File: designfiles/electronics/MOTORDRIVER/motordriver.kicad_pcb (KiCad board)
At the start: 4 copper layers, 416 parts, among them IC1 LM5109BSDX_NOPB, IC10 LM5109BSDX_NOPB, IC11 LM5109BSDX_NOPB, IC12 LM5109BSDX_NOPB, IC13 INA2181A2IDGSR, IC14 LM5109BSDX_NOPB, IC15 LM5109BSDX_NOPB, IC16 LM5109BSDX_NOPB, IC17 LM5109BSDX_NOPB, IC18 INA2181A2IDGSR, IC2 LM5109BSDX_NOPB, IC3 LM5109BSDX_NOPB, IC4 LM5109BSDX_NOPB, IC5 INA2181A2IDGSR, IC6 BQ24133RGYR, IC7 LM5176PWPR, IC8 ATSAME53J18A-MF, IC9 LM5109BSDX_NOPB, J1 IMU1, J2 IMU2, J3 Conn_01x04_Socket, J4 Screw_Terminal_01x02, J5 1-84952-1, J6 1-84952-1, J7 1-84952-1, P1 USB_C_Plug_USB2.0, Q1 30V 71A, Q10 40V 70A, Q11 30V 71A, Q12 30V 71A, Q13 30V 71A, Q14 30V 71A, Q15 30V 71A, Q16 30V 71A, Q17 30V 71A, Q18 30V 71A, Q19 30V 71A, Q2 30V 71A, Q20 30V 71A, Q21 30V 71A, Q22 30V 71A, Q23 30V 71A, Q24 30V 71A, Q25 30V 71A, Q26 30V 71A, Q27 30V 71A, Q28 30V 71A, Q3 30V 71A, Q4 30V 71A, Q5 30V 71A, Q6 30V 71A, Q7 30V 71A, Q8 30V 71A, Q9 30V 71A, SW1 SW_DPST_x2, U1 LD1117S25TR_SOT223, U2 LD1117S33TR_SOT223, U3 LD1117S50TR_SOT223, U4 TMC4671-LA, U5 ATSAMD11D14A-M, U6 TMC4671-LA, U7 TMC4671-LA

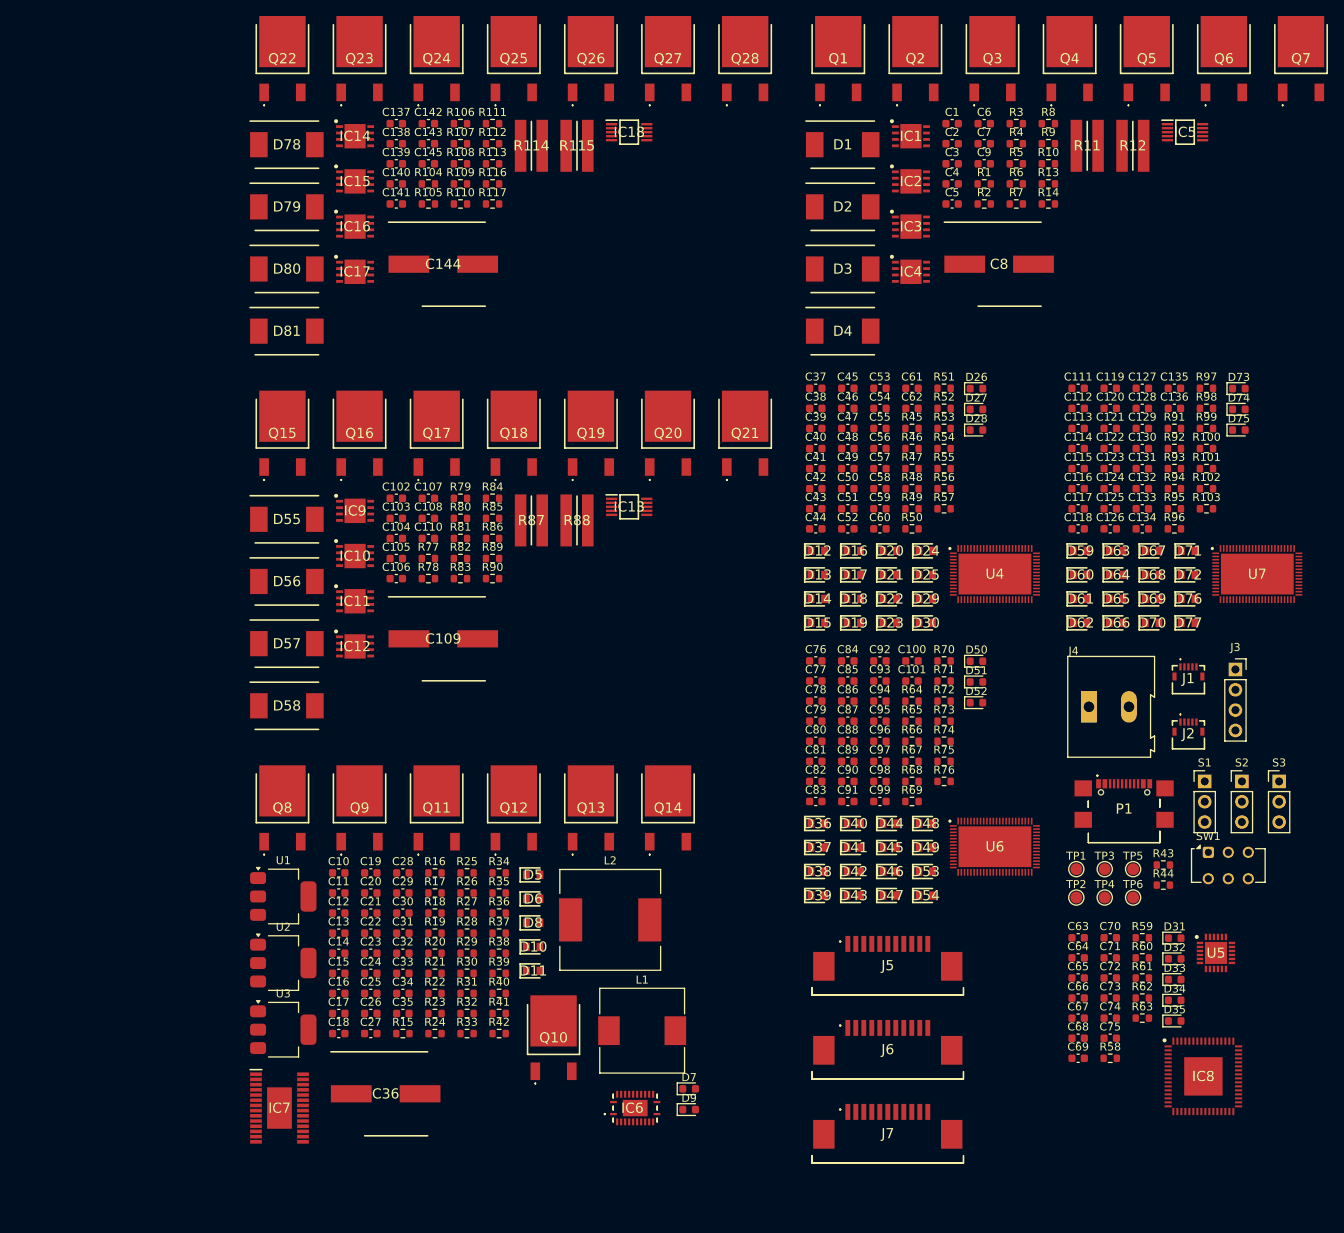
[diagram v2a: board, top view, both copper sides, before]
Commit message: added inductors
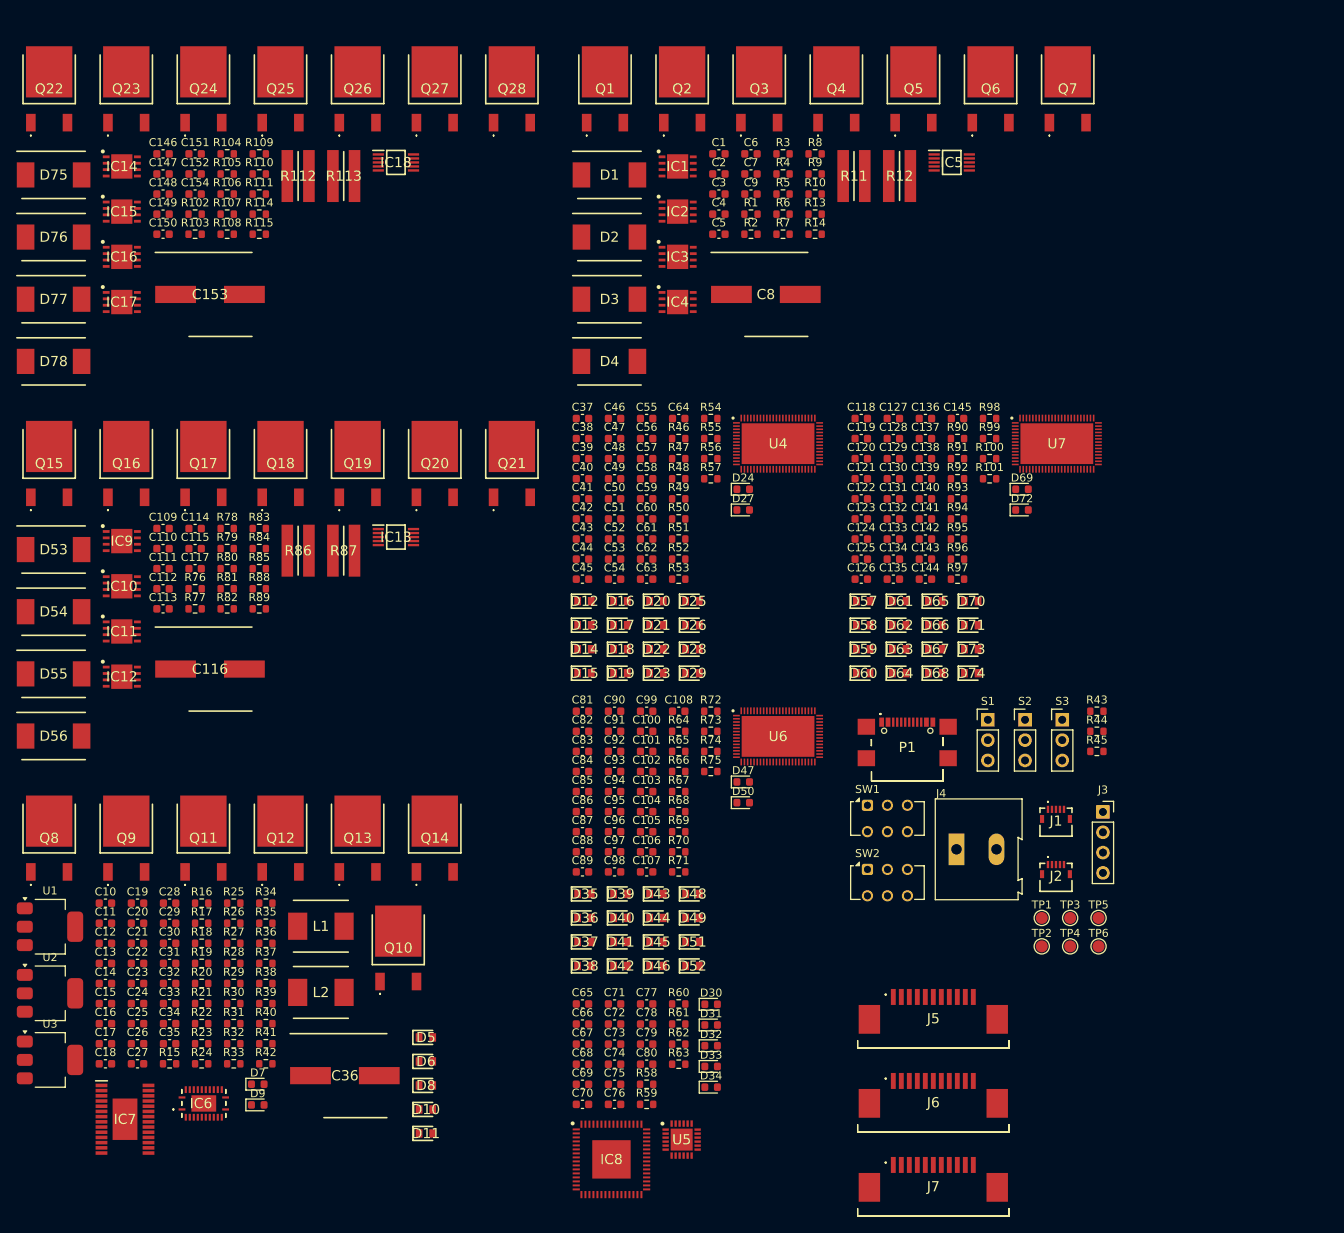
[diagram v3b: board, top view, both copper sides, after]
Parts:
- removed D79, D80, D81: 4A 40V, kuben-footprints:DIOM7959X262N
- removed R116, R117: 0.01Ω, Resistor_SMD:R_0603_1608Metric
- added C146: 0.1µF, Capacitor_SMD:C_0603_1608Metric, F.Cu at (58.1, 37.4)
- added C147: 1µF, Capacitor_SMD:C_0603_1608Metric, F.Cu at (58.1, 40.0)
- added C148: 1µF, Capacitor_SMD:C_0603_1608Metric, F.Cu at (58.1, 42.5)
- added C149: 0.1µF, Capacitor_SMD:C_0603_1608Metric, F.Cu at (58.1, 45.0)
- added C150: 1µF, Capacitor_SMD:C_0603_1608Metric, F.Cu at (58.1, 47.5)
- added C151: 0.1µF, Capacitor_SMD:C_0603_1608Metric, F.Cu at (62.1, 37.4)
- added C152: 1µF, Capacitor_SMD:C_0603_1608Metric, F.Cu at (62.1, 40.0)
- added C153: 220µF 35V, kuben-footprints:CAPAE1050X1050N, F.Cu at (64.0, 55.0)
- added C154: 0.1µF, Capacitor_SMD:C_0603_1608Metric, F.Cu at (62.1, 42.5)
- added SW2: SW_DPST_x2, Button_Switch_THT:SW_CK_JS202011AQN_DPDT_Angled, F.Cu at (146.1, 126.9)
- C100, C123, C127, C131, C59, C75, C90, C94: value 4.7µF -> 100nF
- C101, C62: value 10nF -> 4.7µF
- C102, C105, C142: value 0.1µF -> 470nF
- C103, C108: value 1µF -> 100nF
- C104, C106, C138, C141, C143: value 1µF -> 4.7µF
- C107: value 0.1µF -> 10nF
- C109: value 220µF 35V -> 0.1µF; footprint kuben-footprints:CAPAE1050X1050N -> Capacitor_SMD:C_0603_1608Metric
- C110: value 0.1µF -> 1µF
- C111, C113, C115: value 100nF -> 1µF
- C112, C114, C117: value 100nF -> 0.1µF
- C116: value 100nF -> 220µF 35V; footprint Capacitor_SMD:C_0603_1608Metric -> kuben-footprints:CAPAE1050X1050N
- C118, C120, C121, C46, C83, C86: value 100pF -> 100nF
- C122, C41, C45: value 100nF -> 100pF
- C124, C50, C56: value 470nF -> 100nF
- C125, C88: value 4.7µF -> 100pF
- C126, C89: value 470nF -> 100pF
- C128, C130, C52, C54, C60, C91, C93: value 470nF -> 4.7µF
- C129, C51, C53, C55, C61, C92: value 4.7µF -> 470nF
- C136: value 10nF -> 470nF
- C137, C140, C145: value 0.1µF -> 100nF
- C139: value 1µF -> 470nF
- C144: value 220µF 35V -> 10nF; footprint kuben-footprints:CAPAE1050X1050N -> Capacitor_SMD:C_0603_1608Metric
- C47: value 100pF -> 4.7µF
- C48: value 100nF -> 470nF
- C63: value 100nF -> 10nF
- C64, C68, C70, C72: value 10µF -> 100nF
- C67, C69, C71, C73, C76: value 100nF -> 10µF
- C78: value 100nF -> 4.7µF
- D24, D30, D47, D69, D72: value 4.7Vf 0.5A -> LED; footprint kuben-footprints:DIOC1709X85N -> Diode_SMD:D_0603_1608Metric
- D26, D28, D35, D51, D52, D73, D74: value LED -> 4.7Vf 0.5A; footprint Diode_SMD:D_0603_1608Metric -> kuben-footprints:DIOC1709X85N
- D53, D54, D76, D77: value 4.7Vf 0.5A -> 4A 40V; footprint kuben-footprints:DIOC1709X85N -> kuben-footprints:DIOM7959X262N
- D57, D58: value 4A 40V -> 4.7Vf 0.5A; footprint kuben-footprints:DIOM7959X262N -> kuben-footprints:DIOC1709X85N
- D75: value LED -> 4A 40V; footprint Diode_SMD:D_0603_1608Metric -> kuben-footprints:DIOM7959X262N
- L1: footprint Inductor_SMD:L_10.4x10.4_H4.8 -> kuben-footprints:INDPM6965X300N
- L2: value 1µH 420µΩ -> 1µH 22A; footprint Inductor_SMD:L_12x12mm_H8mm -> kuben-footprints:INDPM6965X300N
- R100: value 10kΩ -> 100kΩ
- R101: value 1kΩ -> 20kΩ
- R102: value 100kΩ -> 5Ω
- R103: value 20kΩ -> 4.7Ω
- R104, R107, R110, R77, R80, R83: value 5Ω -> 4.7Ω
- R105, R108, R79, R82: value 4.7Ω -> 5Ω
- R112, R113, R86: value 4.7Ω -> 10Ω 2W; footprint Resistor_SMD:R_0603_1608Metric -> kuben-footprints:RESC3263X80N
- R114, R115, R88: value 10Ω 2W -> 0.01Ω; footprint kuben-footprints:RESC3263X80N -> Resistor_SMD:R_0603_1608Metric
- R45: value 4.7kΩ -> 10K
- R48: value 1kΩ -> 4.7kΩ
- R51, R73, R97: value 10kΩ -> 1kΩ
- R52, R72, R96, R98: value 1kΩ -> 10kΩ
- R74: value 1kΩ -> 100kΩ
- R75: value 100kΩ -> 20kΩ
- R76: value 20kΩ -> 5Ω
- R90: value 0.01Ω -> 4.7kΩ
- R93: value 4.7kΩ -> 1kΩ
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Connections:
- net /driverIC/ADC_I0_POS renamed /servo1/ADC_I0_POS
- net /driverIC/ADC_I1_POS renamed /servo1/ADC_I1_POS
- net /driverIC/BRAKE renamed /drivergates1/BRAKE
- net /driverIC1/BRAKE renamed /drivergates2/BRAKE
- net /driverIC2/BRAKE renamed /drivergates3/BRAKE
- C100 pad 2: +3.3V -> Net-(U6-VCCCORE2)
- C101 pad 2: Net-(D53-A) -> +3.3V
- C102 pad 1: Net-(IC9-HS) -> GND
- C102 pad 2: Net-(D55-K) -> +3.3V
- C103 pad 1: +12V -> GND
- C103 pad 2: GND -> Net-(U6-VCCCORE1)
- C104 pad 1: +12V -> GND
- C104 pad 2: GND -> +3.3V
- C105 pad 1: Net-(IC10-HS) -> GND
- C105 pad 2: Net-(D56-K) -> +3.3V
- C106 pad 1: +12V -> GND
- C106 pad 2: GND -> +5V
- C107 pad 1: Net-(IC12-HS) -> GND
- C107 pad 2: Net-(D57-K) -> Net-(D51-A)
- C108 pad 1: +12V -> GND
- C108 pad 2: GND -> +5V
- C109 pad 1: +12V -> Net-(IC9-HS)
- C109 pad 2: GND -> Net-(D53-K)
- C110 pad 1: GND -> +12V
- C110 pad 2: +5V -> GND
- C111 pad 1: GND -> +12V
- C111 pad 2: +3.3V -> GND
- C112 pad 1: GND -> Net-(IC10-HS)
- C112 pad 2: +3.3V -> Net-(D54-K)
- C113 pad 1: GND -> +12V
- C113 pad 2: +3.3V -> GND
- C114 pad 1: GND -> Net-(IC12-HS)
- C114 pad 2: +3.3V -> Net-(D55-K)
- C115 pad 1: GND -> +12V
- C115 pad 2: +3.3V -> GND
- C116 pad 1: GND -> +12V
- C116 pad 2: +3.3V -> GND
- C117 pad 2: +3.3V -> +5V
- C118 pad 2: /driverIC2/HALL_U -> +3.3V
- C120 pad 2: /driverIC2/HALL_V -> +3.3V
- C121 pad 2: /driverIC2/HALL_W -> +3.3V
- C122 pad 2: +3.3V -> /servo3/HALL_U
- C124 pad 2: +3.3V -> Net-(U7-VCCCORE3)
- C125 pad 2: +3.3V -> /servo3/HALL_V
- C126 pad 2: +3.3V -> /servo3/HALL_W
- C131 pad 1: GND -> Net-(U7-NRST)
- C131 pad 2: +3.3V -> GND
- C136 pad 2: Net-(D76-A) -> +3.3V
- C137 pad 1: Net-(IC14-HS) -> GND
- C137 pad 2: Net-(D78-K) -> Net-(U7-VCCCORE2)
- C138 pad 1: +12V -> GND
- C138 pad 2: GND -> +3.3V
- C139 pad 1: +12V -> GND
- C139 pad 2: GND -> +3.3V
- C140 pad 1: Net-(IC15-HS) -> GND
- C140 pad 2: Net-(D79-K) -> Net-(U7-VCCCORE1)
- C141 pad 1: +12V -> GND
- C141 pad 2: GND -> +3.3V
- C142 pad 1: Net-(IC17-HS) -> GND
- C142 pad 2: Net-(D80-K) -> +3.3V
- C143 pad 1: +12V -> GND
- C143 pad 2: GND -> +5V
- C144 pad 1: +12V -> GND
- C144 pad 2: GND -> Net-(D73-A)
- C41 pad 2: +3.3V -> /servo1/HALL_U
- C43 pad 2: +3.3V -> Net-(U4-VCCCORE3)
- C44 pad 2: /driverIC/HALL_U -> /servo1/HALL_V
- C45 pad 2: +3.3V -> /servo1/HALL_W
- C46 pad 2: /driverIC/HALL_V -> +3.3V
- C47 pad 2: /driverIC/HALL_W -> +3.3V
- C50 pad 1: GND -> Net-(U4-NRST)
- C50 pad 2: +3.3V -> GND
- C56 pad 2: +3.3V -> Net-(U4-VCCCORE2)
- C59 pad 2: +3.3V -> Net-(U4-VCCCORE1)
- C62 pad 2: Net-(D29-A) -> +5V
- C63 pad 1: +3.3V -> GND
- C63 pad 2: GND -> Net-(D28-A)
- C64 pad 1: +3.3V -> GND
- C64 pad 2: GND -> +5V
- C74 pad 1: Net-(IC8-VDDCORE) -> +3.3V
- C75 pad 1: Net-(IC8-VDDCORE) -> +3.3V
- C76 pad 1: GND -> +3.3V
- C76 pad 2: +3.3V -> GND
- C77 pad 2: +3.3V -> Net-(IC8-VDDCORE)
- C78 pad 2: +3.3V -> Net-(IC8-VDDCORE)
- C79 pad 1: GND -> /IO/RESETN
- C79 pad 2: +3.3V -> GND
- C80 pad 1: GND -> +3.3V
- C80 pad 2: +3.3V -> GND
- C83 pad 2: /driverIC1/HALL_U -> +3.3V
- C85 pad 2: /driverIC1/HALL_V -> /servo2/HALL_U
- C86 pad 2: /driverIC1/HALL_W -> +3.3V
- C87 pad 2: +3.3V -> Net-(U6-VCCCORE3)
- C88 pad 2: +3.3V -> /servo2/HALL_V
- C89 pad 2: +3.3V -> /servo2/HALL_W
- C94 pad 1: GND -> Net-(U6-NRST)
- C94 pad 2: +3.3V -> GND
- D20 pad 2: /driverIC/HALL_W -> /servo1/HALL_W
- D21 pad 1: /driverIC/HALL_W -> /servo1/HALL_W
- D22 pad 2: /driverIC/HALL_V -> /servo1/HALL_V
- D23 pad 1: /driverIC/HALL_V -> /servo1/HALL_V
- D24 pad 1: +5V -> GND
- D24 pad 2: /driverIC/HALL_U -> Net-(D24-A)
- D25 pad 1: /driverIC/HALL_U -> +5V
- D25 pad 2: GND -> /servo1/HALL_U
- D26 pad 1: GND -> /servo1/HALL_U
- D26 pad 2: Net-(D26-A) -> GND
- D28 pad 1: GND -> +5V
- D29 pad 1: +5V -> Net-(D28-A)
- D29 pad 2: Net-(D29-A) -> GND
- D30 pad 1: Net-(D29-A) -> GND
- D30 pad 2: GND -> Net-(D30-A)
- D35 pad 1: GND -> +5V
- D35 pad 2: Net-(D35-A) -> /servo2/ADC_I0_POS
- D36 pad 1: +5V -> /servo2/ADC_I0_POS
- D36 pad 2: /driverIC1/ADC_I0_POS -> GND
- D37 pad 1: /driverIC1/ADC_I0_POS -> +5V
- D37 pad 2: GND -> /servo2/ADC_I1_POS
- D38 pad 1: +5V -> /servo2/ADC_I1_POS
- D38 pad 2: /driverIC1/ADC_I1_POS -> GND
- D39 pad 1: /driverIC1/ADC_I1_POS -> +5V
- D39 pad 2: GND -> +2.5V
- D40 pad 1: +5V -> +2.5V
- D40 pad 2: +2.5V -> GND
- D41 pad 1: +2.5V -> +5V
- D41 pad 2: GND -> +2.5V
- D42 pad 1: +5V -> +2.5V
- D42 pad 2: +2.5V -> GND
- D43 pad 1: +2.5V -> +5V
- D43 pad 2: GND -> /servo2/HALL_W
- D44 pad 1: +5V -> /servo2/HALL_W
- D44 pad 2: /driverIC1/HALL_W -> GND
- D45 pad 1: /driverIC1/HALL_W -> +5V
- D45 pad 2: GND -> /servo2/HALL_V
- D46 pad 1: +5V -> /servo2/HALL_V
- D46 pad 2: /driverIC1/HALL_V -> GND
- D47 pad 1: /driverIC1/HALL_V -> GND
- D47 pad 2: GND -> Net-(D47-A)
- D48 pad 2: /driverIC1/HALL_U -> /servo2/HALL_U
- D49 pad 1: /driverIC1/HALL_U -> /servo2/HALL_U
- D51 pad 1: GND -> +5V
- D52 pad 1: GND -> Net-(D51-A)
- D52 pad 2: Net-(D52-A) -> GND
- D53 pad 1: +5V -> Net-(D53-K)
- D54 pad 1: Net-(D53-A) -> Net-(D54-K)
- D54 pad 2: GND -> Net-(D54-A)
- D56 pad 1: Net-(D56-K) -> +12V
- D57 pad 1: Net-(D57-K) -> +5V
- D57 pad 2: Net-(D57-A) -> /servo3/ADC_I0_POS
- D58 pad 1: +12V -> /servo3/ADC_I0_POS
- D58 pad 2: Net-(D58-A) -> GND
- D59 pad 2: /driverIC2/ADC_I0_POS -> /servo3/ADC_I1_POS
- D60 pad 1: /driverIC2/ADC_I0_POS -> /servo3/ADC_I1_POS
- D61 pad 2: /driverIC2/ADC_I1_POS -> +2.5V
- D62 pad 1: /driverIC2/ADC_I1_POS -> +2.5V
- D65 pad 2: +2.5V -> /servo3/HALL_W
- D66 pad 1: +2.5V -> /servo3/HALL_W
- D67 pad 2: /driverIC2/HALL_W -> /servo3/HALL_V
- D68 pad 1: /driverIC2/HALL_W -> /servo3/HALL_V
- D69 pad 1: +5V -> GND
- D69 pad 2: /driverIC2/HALL_V -> Net-(D69-A)
- D70 pad 1: /driverIC2/HALL_V -> +5V
- D70 pad 2: GND -> /servo3/HALL_U
- D71 pad 1: +5V -> /servo3/HALL_U
- D71 pad 2: /driverIC2/HALL_U -> GND
- D72 pad 1: /driverIC2/HALL_U -> GND
- D72 pad 2: GND -> Net-(D72-A)
- D73 pad 1: GND -> +5V
- D74 pad 1: GND -> Net-(D73-A)
- D74 pad 2: Net-(D74-A) -> GND
- D75 pad 1: GND -> Net-(D75-K)
- D76 pad 1: +5V -> Net-(D76-K)
- D77 pad 1: Net-(D76-A) -> Net-(D77-K)
- D77 pad 2: GND -> Net-(D77-A)
- D78 pad 1: Net-(D78-K) -> +12V
- IC1 pad 2: /drivergates/PWM_W_H -> /drivergates1/PWM_W_H
- IC1 pad 3: /drivergates/PWM_W_L -> /drivergates1/PWM_W_L
- IC10 pad 2: /drivergates1/PWM_V_H -> /drivergates2/PWM_V_H
- IC10 pad 3: /drivergates1/PWM_V_L -> /drivergates2/PWM_V_L
- IC10 pad 8: Net-(D56-K) -> Net-(D54-K)
- IC12 pad 2: /drivergates1/PWM_U_H -> /drivergates2/PWM_U_H
- IC12 pad 3: /drivergates1/PWM_U_L -> /drivergates2/PWM_U_L
- IC12 pad 8: Net-(D57-K) -> Net-(D55-K)
- IC13 pad 1: /driverIC1/ADC_I0_POS -> /servo2/ADC_I0_POS
- IC13 pad 9: /driverIC1/ADC_I1_POS -> /servo2/ADC_I1_POS
- IC14 pad 2: /drivergates2/PWM_W_H -> /drivergates3/PWM_W_H
- IC14 pad 3: /drivergates2/PWM_W_L -> /drivergates3/PWM_W_L
- IC14 pad 8: Net-(D78-K) -> Net-(D75-K)
- IC15 pad 2: /drivergates2/PWM_V_H -> /drivergates3/PWM_V_H
- IC15 pad 3: /drivergates2/PWM_V_L -> /drivergates3/PWM_V_L
- IC15 pad 8: Net-(D79-K) -> Net-(D76-K)
- IC17 pad 2: /drivergates2/PWM_U_H -> /drivergates3/PWM_U_H
- IC17 pad 3: /drivergates2/PWM_U_L -> /drivergates3/PWM_U_L
- IC17 pad 8: Net-(D80-K) -> Net-(D77-K)
- IC18 pad 1: /driverIC2/ADC_I0_POS -> /servo3/ADC_I0_POS
- IC18 pad 9: /driverIC2/ADC_I1_POS -> /servo3/ADC_I1_POS
- IC2 pad 2: /drivergates/PWM_V_H -> /drivergates1/PWM_V_H
- IC2 pad 3: /drivergates/PWM_V_L -> /drivergates1/PWM_V_L
- IC4 pad 2: /drivergates/PWM_U_H -> /drivergates1/PWM_U_H
- IC4 pad 3: /drivergates/PWM_U_L -> /drivergates1/PWM_U_L
- IC8 pad 1: /microcontrollers/SDA_IMU1 -> /microcontrollers/PROCLED
- IC8 pad 10: /microcontrollers/STATUS3 -> /IO/INT1 IMU1
- IC8 pad 11: /microcontrollers/SDA_IMU2 -> unconnected-(IC8-PB08-Pad11)
- IC8 pad 12: /microcontrollers/SCL_IMU2 -> unconnected-(IC8-PB09-Pad12)
- IC8 pad 13: /microcontrollers/SERVO1_RX -> unconnected-(IC8-PA04-Pad13)
- IC8 pad 14: /microcontrollers/SERVO1_TX -> unconnected-(IC8-PA05-Pad14)
- IC8 pad 15: /microcontrollers/SERVO3_RX -> unconnected-(IC8-PA06-Pad15)
- IC8 pad 16: /microcontrollers/SERVO3_TX -> unconnected-(IC8-PA07-Pad16)
- IC8 pad 17: /IO/OLED_SCL -> /IO/SDA IMU1
- IC8 pad 18: /IO/OLED_SDA -> /IO/SCL IMU1
- IC8 pad 19: /microcontrollers/SERVO2_TX -> unconnected-(IC8-PA10-Pad19)
- IC8 pad 2: /microcontrollers/SCL_IMU1 -> /microcontrollers/ERRLED
- IC8 pad 20: /microcontrollers/SERVO1_PWM -> unconnected-(IC8-PA11-Pad20)
- IC8 pad 23: /microcontrollers/SERVO1_CLK -> SERVO_CLK
- IC8 pad 24: /microcontrollers/SERVO1_ENI -> SERVO_ENI
- IC8 pad 25: /microcontrollers/SERVO2_RX -> /microcontrollers/SERVO1_PWM_I
- IC8 pad 26: SPI_SCK -> /microcontrollers/SERVO2_PWM_I
- IC8 pad 27: SPI_MOSI -> /microcontrollers/SERVO3_PWM_I
- IC8 pad 28: SPI_MISO -> /IO/BRAKE1
- IC8 pad 29: /microcontrollers/SERVO2_PWM -> /IO/BRAKE2
- IC8 pad 3: /microcontrollers/SERVO1_STATUS -> unconnected-(IC8-PA02-Pad3)
- IC8 pad 30: /microcontrollers/SERVO3_GPIO2 -> /IO/RX
- IC8 pad 31: /microcontrollers/INT1_IMU2 -> /IO/TX
- IC8 pad 32: /microcontrollers/INT1_IMU1 -> /IO/BRAKE3
- IC8 pad 35: unconnected-(IC8-PA16-Pad35) -> /IO/SDA IMU2
- IC8 pad 36: /microcontrollers/BRAKE3 -> /IO/SCL IMU2
- IC8 pad 37: /microcontrollers/BRAKE2 -> unconnected-(IC8-PA18-Pad37)
- IC8 pad 38: /microcontrollers/BRAKE1 -> unconnected-(IC8-PA19-Pad38)
- IC8 pad 39: /microcontrollers/SERVO3_CS -> TMC_DB_MISO
- IC8 pad 4: /microcontrollers/SERVO2_STATUS -> /microcontrollers/SERVO1_STATUS
- IC8 pad 40: /microcontrollers/SERVO2_CS -> TMC_DB_MOSI
- IC8 pad 41: /microcontrollers/SERVO1_CS -> TMC_DB_SCK
- IC8 pad 42: /microcontrollers/RX -> SPI_SCK
- IC8 pad 43: /microcontrollers/TX -> /IO/OLED_SDA
- IC8 pad 44: unconnected-(IC8-PA23-Pad44) -> /IO/OLED_SCL
- IC8 pad 45: /microcontrollers/SERVO3_GPIO1 -> SPI_MISO
- IC8 pad 46: /microcontrollers/SERVO3_GPIO0 -> SPI_MOSI
- IC8 pad 49: /microcontrollers/SERVO2_GPIO2 -> /microcontrollers/STATUS1
- IC8 pad 5: /microcontrollers/SERVO3_STATUS -> /microcontrollers/SERVO2_STATUS
- IC8 pad 50: /microcontrollers/SERVO2_GPIO1 -> /microcontrollers/STATUS2
- IC8 pad 51: /microcontrollers/SERVO2_GPIO0 -> /microcontrollers/STATUS3
- IC8 pad 52: /microcontrollers/RESETN -> /IO/RESETN
- IC8 pad 59: /microcontrollers/SERVO1_GPIO2 -> /microcontrollers/SERVO1_DB_CS
- IC8 pad 6: /microcontrollers/STATUS1 -> /microcontrollers/SERVO3_STATUS
- IC8 pad 60: /microcontrollers/SERVO1_GPIO1 -> /microcontrollers/SERVO2_DB_CS
- IC8 pad 61: /microcontrollers/SERVO1_GPIO0 -> /microcontrollers/SERVO3_DB_CS
- IC8 pad 62: /microcontrollers/PROCLED -> /microcontrollers/SERVO3_CS
- IC8 pad 63: /microcontrollers/SERVO3_PWM_I -> /microcontrollers/SERVO2_CS
- IC8 pad 64: /microcontrollers/ERRLED -> /microcontrollers/SERVO1_CS
- IC8 pad 9: /microcontrollers/STATUS2 -> /IO/INT1 IMU2
- IC9 pad 2: /drivergates1/PWM_W_H -> /drivergates2/PWM_W_H
- IC9 pad 3: /drivergates1/PWM_W_L -> /drivergates2/PWM_W_L
- IC9 pad 8: Net-(D55-K) -> Net-(D53-K)
- J5 pad 1: /drivergates2/PHASE_U -> /drivergates3/PHASE_U
- J5 pad 10: /motorIO/HALL_C1 -> /servo3/HALL_W
- J5 pad 2: /drivergates2/PHASE_U -> /drivergates3/PHASE_U
- J5 pad 3: /drivergates2/PHASE_V -> /drivergates3/PHASE_V
- J5 pad 4: /drivergates2/PHASE_V -> /drivergates3/PHASE_V
- J5 pad 5: /drivergates2/PHASE_W -> /drivergates3/PHASE_W
- J5 pad 6: /drivergates2/PHASE_W -> /drivergates3/PHASE_W
- J5 pad 8: /driverIC2/HALL_V -> /servo3/HALL_V
- J5 pad 9: /motorIO/HALL_A1 -> /servo3/HALL_U
- J6 pad 1: /drivergates1/PHASE_U -> /drivergates2/PHASE_U
- J6 pad 10: /motorIO/HALL_C2 -> /servo2/HALL_W
- J6 pad 2: /drivergates1/PHASE_U -> /drivergates2/PHASE_U
- J6 pad 3: /drivergates1/PHASE_V -> /drivergates2/PHASE_V
- J6 pad 4: /drivergates1/PHASE_V -> /drivergates2/PHASE_V
- J6 pad 5: /drivergates1/PHASE_W -> /drivergates2/PHASE_W
- J6 pad 6: /drivergates1/PHASE_W -> /drivergates2/PHASE_W
- J6 pad 8: /driverIC1/HALL_V -> /servo2/HALL_V
- J6 pad 9: /motorIO/HALL_A2 -> /servo2/HALL_U
- J7 pad 1: /drivergates/PHASE_U -> /drivergates1/PHASE_U
- J7 pad 10: /motorIO/HALL_C3 -> /servo1/HALL_W
- J7 pad 2: /drivergates/PHASE_U -> /drivergates1/PHASE_U
- J7 pad 3: /drivergates/PHASE_V -> /drivergates1/PHASE_V
- J7 pad 4: /drivergates/PHASE_V -> /drivergates1/PHASE_V
- J7 pad 5: /drivergates/PHASE_W -> /drivergates1/PHASE_W
- J7 pad 6: /drivergates/PHASE_W -> /drivergates1/PHASE_W
- J7 pad 8: /driverIC/HALL_V -> /servo1/HALL_V
- J7 pad 9: /motorIO/HALL_A3 -> /servo1/HALL_U
- Q15 pad 2: Net-(D58-A) -> Net-(D56-A)
- Q20 pad 3: /drivergates1/PHASE_W -> /drivergates2/PHASE_W
- Q21 pad 2: /drivergates1/PHASE_W -> /drivergates2/PHASE_W
- Q22 pad 2: Net-(D81-A) -> Net-(D78-A)
- Q27 pad 3: /drivergates2/PHASE_W -> /drivergates3/PHASE_W
- Q28 pad 2: /drivergates2/PHASE_W -> /drivergates3/PHASE_W
- Q6 pad 3: /drivergates/PHASE_W -> /drivergates1/PHASE_W
- Q7 pad 2: /drivergates/PHASE_W -> /drivergates1/PHASE_W
- R100 pad 1: Net-(U7-NRST) -> +12V
- R100 pad 2: +3.3V -> Net-(D73-A)
- R101 pad 1: Net-(D75-A) -> Net-(D73-A)
- R101 pad 2: Net-(U7-GPIO7_/_AENC_WY_MCD_/_DBGSPI_TRG) -> GND
- R102 pad 2: Net-(D76-A) -> Net-(D75-A)
- R103 pad 1: Net-(D76-A) -> Net-(IC14-HO)
- R103 pad 2: GND -> Net-(Q27-G)
- R104 pad 1: +12V -> Net-(Q28-G)
- R104 pad 2: Net-(D78-A) -> Net-(IC14-LO)
- R105 pad 1: Net-(IC14-HO) -> +12V
- R105 pad 2: Net-(Q27-G) -> Net-(D76-A)
- R106 pad 1: Net-(Q28-G) -> Net-(IC15-HO)
- R106 pad 2: Net-(IC14-LO) -> Net-(Q25-G)
- R107 pad 1: +12V -> Net-(Q26-G)
- R107 pad 2: Net-(D79-A) -> Net-(IC15-LO)
- R108 pad 1: Net-(IC15-HO) -> +12V
- R108 pad 2: Net-(Q25-G) -> Net-(D77-A)
- R109 pad 1: Net-(Q26-G) -> Net-(IC17-HO)
- R109 pad 2: Net-(IC15-LO) -> Net-(Q23-G)
- R110 pad 1: +12V -> Net-(Q22-G)
- R110 pad 2: Net-(D80-A) -> Net-(IC16-LO)
- R111 pad 1: Net-(IC17-HO) -> Net-(Q24-G)
- R111 pad 2: Net-(Q23-G) -> Net-(IC17-LO)
- R112 pad 1: Net-(Q22-G) -> +12V
- R112 pad 2: Net-(IC16-LO) -> Net-(D78-A)
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
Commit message: minor tweaks on schematic and started on the pcb layout, made good work
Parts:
- removed SW2: SW_DPST_x2, Button_Switch_THT:SW_CK_JS202011AQN_DPDT_Angled
- C1, C100, C101, C102, C103, C104, C105, C106, C107, C108, C109, C110, C111, C112, C113, C114, C115, C116, C117, C118, C119, C120, C121, C122, C123, C124, C125, C126, C127, C128, C129, C130, C131, C132, C133, C134, C135, C136, C137, C138, C139, C140, C141, C142, C143, C144, C145, C146, C147, C148, C149, C150, C151, C152, C153, C154, C2, C3, C36, C37, C38, C39, C4, C40, C41, C42, C43, C44, C45, C46, C47, C48, C49, C5, C50, C51, C52, C53, C54, C55, C56, C57, C58, C59, C6, C60, C61, C62, C63, C64, C7, C8, C81, C82, C83, C84, C85, C86, C87, C88, C89, C9, C90, C91, C92, C93, C94, C95, C96, C97, C98, C99, D1, D12, D13, D14, D15, D16, D17, D18, D19, D2, D20, D21, D22, D23, D24, D25, D26, D27, D28, D29, D3, D35, D36, D37, D38, D39, D4, D40, D41, D42, D43, D44, D45, D46, D47, D48, D49, D50, D51, D52, D53, D54, D55, D56, D57, D58, D59, D60, D61, D62, D63, D64, D65, D66, D67, D68, D69, D70, D71, D72, D73, D74, D75, D76, D77, D78, IC1, IC10, IC11, IC12, IC13, IC14, IC15, IC16, IC17, IC18, IC2, IC3, IC4, IC5, IC9, J1, J2, J5, J6, J7, Q1, Q15, Q16, Q17, Q18, Q19, Q2, Q20, Q21, Q22, Q23, Q24, Q25, Q26, Q27, Q28, Q3, Q4, Q5, Q6, Q7, R1, R10, R100, R101, R102, R103, R104, R105, R106, R107, R108, R109, R11, R110, R111, R112, R113, R114, R115, R12, R13, R14, R2, R3, R4, R46, R47, R48, R49, R5, R50, R51, R52, R53, R54, R55, R56, R57, R6, R64, R65, R66, R67, R68, R69, R7, R70, R71, R72, R73, R74, R75, R76, R77, R78, R79, R8, R80, R81, R82, R83, R84, R85, R86, R87, R88, R89, R9, R90, R91, R92, R93, R94, R95, R96, R97, R98, R99, S1, S2, S3, U4, U6, U7: moved to B.Cu
- J4: value Screw_Terminal_01x02 -> XT60-M; footprint TerminalBlock:TerminalBlock_Altech_AK300-2_P5.00mm -> kuben-footprints:AMASS_XT60-M; moved to B.Cu
- SW1: value SW_DPST_x2 -> PUSH; footprint Button_Switch_THT:SW_CK_JS202011AQN_DPDT_Angled -> Button_Switch_THT:SW_PUSH_6mm
- moved C67 189.1 mm to (218.0, 304.3), turned to -90 degrees
- moved C68 187.9 mm to (219.5, 304.3), turned to -90 degrees
- moved C71 187.4 mm to (229.5, 291.8)
- moved C72 186.7 mm to (229.5, 293.3)
- moved C73 185.9 mm to (229.5, 294.8)
- moved C74 185.1 mm to (229.5, 296.3)
- moved C65 179.3 mm to (217.9, 287.2), turned to 90 degrees
- moved R60 178.4 mm to (231.0, 285.3), turned to -90 degrees
- moved C66 178.2 mm to (219.4, 287.3), turned to 90 degrees
- moved C77 177.3 mm to (222.6, 287.3), turned to -90 degrees
- moved R61 174.8 mm to (228.4, 285.3), turned to -90 degrees
- moved C78 174.4 mm to (221.0, 287.3), turned to -90 degrees
- moved C79 174.2 mm to (224.1, 287.3), turned to 90 degrees
- moved C69 173.1 mm to (211.4, 294.4), turned to 180 degrees
- moved C70 172.4 mm to (211.4, 296.0), turned to 180 degrees
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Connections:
- IC8 pad 25: /microcontrollers/SERVO1_PWM_I -> TMC_DB_MISO
- IC8 pad 26: /microcontrollers/SERVO2_PWM_I -> TMC_DB_MOSI
- IC8 pad 27: /microcontrollers/SERVO3_PWM_I -> TMC_DB_SCK
- IC8 pad 28: /IO/BRAKE1 -> unconnected-(IC8-PB15-Pad28)
- IC8 pad 29: /IO/BRAKE2 -> /IO/OLED_SDA
- IC8 pad 30: /IO/RX -> /IO/OLED_SCL
- IC8 pad 31: /IO/TX -> unconnected-(IC8-PA14-Pad31)
- IC8 pad 37: unconnected-(IC8-PA18-Pad37) -> /IO/RX
- IC8 pad 38: unconnected-(IC8-PA19-Pad38) -> /IO/TX
- IC8 pad 39: TMC_DB_MISO -> /IO/BRAKE1
- IC8 pad 40: TMC_DB_MOSI -> /IO/BRAKE2
- IC8 pad 41: TMC_DB_SCK -> /microcontrollers/SERVO1_PWM_I
- IC8 pad 42: SPI_SCK -> /microcontrollers/SERVO2_PWM_I
- IC8 pad 43: /IO/OLED_SDA -> /microcontrollers/SERVO3_PWM_I
- IC8 pad 44: /IO/OLED_SCL -> SPI_SCK
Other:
- board outline added: 140 x 140 mm

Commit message: worked on PCB
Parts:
- added H1: MountingHole, MountingHole:MountingHole_3.2mm_M3_DIN965_Pad, F.Cu at (83.9, 27.0)
- added H2: MountingHole, MountingHole:MountingHole_3.2mm_M3_DIN965_Pad, F.Cu at (83.6, 157.2)
- added H3: MountingHole, MountingHole:MountingHole_3.2mm_M3_DIN965_Pad, F.Cu at (213.0, 27.2)
- added H4: MountingHole, MountingHole:MountingHole_3.2mm_M3_DIN965_Pad, F.Cu at (213.3, 156.5)
- added J8: IMU2, kuben-footprints:59453052110ECHLF, B.Cu at (175.0, 76.6)
- C100, C101, C102, C103, C104, C105, C106, C107, C108, C118, C119, C120, C121, C122, C123, C124, C125, C126, C127, C128, C129, C130, C131, C132, C133, C134, C135, C136, C137, C138, C139, C140, C141, C142, C143, C144, C145, C37, C38, C39, C40, C41, C42, C43, C44, C45, C46, C47, C48, C49, C50, C51, C52, C53, C54, C55, C56, C57, C58, C59, C60, C61, C62, C63, C64, C81, C82, C83, C84, C85, C86, C87, C88, C89, C90, C91, C92, C93, C94, C95, C96, C97, C98, C99, D12, D13, D14, D15, D16, D17, D18, D19, D20, D21, D22, D23, D24, D25, D26, D27, D28, D29, D35, D36, D37, D38, D39, D40, D41, D42, D43, D44, D45, D46, D47, D48, D49, D50, D51, D52, D57, D58, D59, D60, D61, D62, D63, D64, D65, D66, D67, D68, D69, D70, D71, D72, D73, D74, R100, R101, R46, R47, R48, R49, R50, R51, R52, R53, R54, R55, R56, R57, R64, R65, R66, R67, R68, R69, R70, R71, R72, R73, R74, R75, R90, R91, R92, R93, R94, R95, R96, R97, R98, R99, U4, U6, U7: moved to F.Cu
- moved D9 231.5 mm to (114.9, 54.2)
- moved C26 229.3 mm to (169.6, 50.8)
- moved C27 229.3 mm to (169.6, 53.4)
- moved C16 229.3 mm to (165.6, 48.3)
- moved C25 229.3 mm to (169.6, 48.3)
- moved R32 227.1 mm to (116.2, 50.5)
- moved C20 224.1 mm to (146.7, 38.0)
- moved C21 224.1 mm to (146.7, 40.5)
- moved C22 224.1 mm to (146.7, 43.0)
- moved C23 224.1 mm to (146.7, 45.5)
- moved C24 224.1 mm to (146.7, 48.0)
- moved R19 224.1 mm to (154.7, 43.0)
- moved R29 224.1 mm to (158.7, 45.5)
- moved R30 224.1 mm to (158.7, 48.0)
- moved C10 224.1 mm to (142.7, 35.5)
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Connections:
- net /IO/SCL IMU1 renamed /IO/SCL_IMU1
- net /IO/SCL IMU2 renamed /IO/SCL_IMU2
- net /IO/SDA IMU1 renamed /IO/SDA_IMU1
- net /IO/SDA IMU2 renamed /IO/SDA_IMU2
- IC8 pad 10: /IO/INT1 IMU1 -> /IO/INT_IMU2
- IC8 pad 11: unconnected-(IC8-PB08-Pad11) -> /IO/INT_IMU3
- IC8 pad 9: /IO/INT1 IMU2 -> /IO/INT_IMU1
- J1 pad 5: /IO/INT1 IMU1 -> /IO/INT_IMU1
- J2 pad 5: /IO/INT1 IMU2 -> /IO/INT_IMU2
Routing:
- added copper zone on B.Cu, net +12V
- added copper zone on F.Cu, net GND
- added copper zone on In2.Cu, net GND

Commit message: worked on PCB
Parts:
- removed J8: IMU2, kuben-footprints:59453052110ECHLF
- H1, H2, H3, H4: value MountingHole -> MountingHole_Pad
- moved J1 291.4 mm to (481.7, 104.0)
- moved L2 272.9 mm to (423.3, 94.1)
- moved Q2 272.9 mm to (412.2, 89.2)
- moved Q3 272.9 mm to (412.2, 98.8)
- moved Q4 272.9 mm to (434.4, 98.8)
- moved Q5 272.9 mm to (434.4, 89.2)
- moved Q7 260.5 mm to (439.3, 59.6)
- moved C41 260.5 mm to (431.4, 64.3)
- moved C43 260.5 mm to (431.4, 61.1)
- moved Q6 260.5 mm to (439.4, 50.9)
- moved C42 260.5 mm to (431.3, 62.7)
- moved R20 260.5 mm to (442.7, 64.9)
- moved R22 260.5 mm to (431.4, 59.6)
- moved R46 260.5 mm to (434.6, 67.9)
- moved R47 260.5 mm to (434.6, 66.3)
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- renumbered C20 to C1, C16 to C10, C108 to C100, C106 to C101, C107 to C102, C105 to C103, C92 to C104, C88 to C105, C89 to C106, C85 to C107, C82 to C108, C74 to C109, C26 to C11, C70 to C110, C73 to C111, C80 to C112, C65 to C113, C66 to C114, C71 to C115, C77 to C116, C72 to C117, C69 to C118, C79 to C119, C27 to C12, C78 to C120, C144 to C121, C126 to C122, C122 to C123, C125 to C124, C75 to C125, C76 to C126, C9 to C127, C8 to C128, C3 to C129, C58 to C13, C7 to C130, C2 to C131, C5 to C132, C6 to C133, C1 to C134, C4 to C135, C154 to C136, C152 to C137, C151 to C138, C153 to C139, C59 to C14, C36 to C140, C148 to C141, C150 to C142, C117 to C143, C146 to C144, C147 to C145, C149 to C146, C111 to C147, C113 to C148, C115 to C149, C53 to C15, C112 to C150, C114 to C151, C116 to C152, C110 to C153, C109 to C154, C55 to C16, C61 to C17, C60 to C18, C62 to C19, C28 to C2, C54 to C20, C57 to C21, C40 to C22, C46 to C23, C42 to C24, C47 to C25, C43 to C26, C64 to C27, C51 to C28, C48 to C29, C10 to C3, C37 to C30, C38 to C31, C52 to C32, C50 to C33, C39 to C34, C49 to C35, C12 to C36, C56 to C37, C18 to C38, C14 to C39, C24 to C4, C15 to C40, C17 to C41, C19 to C42, C11 to C43, C97 to C44, C102 to C45, C86 to C46, C104 to C47, C98 to C48, C101 to C49, C23 to C5, C63 to C50, C99 to C51, C91 to C52, C87 to C53, C90 to C54, C84 to C55, C29 to C56, C95 to C57, C96 to C58, C32 to C59, C22 to C6, C94 to C60, C41 to C61, C81 to C62, C33 to C63, C83 to C64, C31 to C65, C45 to C66, C30 to C67, C93 to C68, C44 to C69, C13 to C7, C100 to C70, C68 to C71, C35 to C72, C34 to C73, C67 to C74, C124 to C75, C136 to C76, C121 to C77, C145 to C78, C119 to C79, C21 to C8, C142 to C80, C131 to C81, C130 to C82, C118 to C83, C133 to C84, C135 to C85, C129 to C86, C123 to C87, C120 to C88, C137 to C89, C25 to C9, C140 to C90, C143 to C91, C138 to C92, C141 to C93, C127 to C94, C139 to C95, C134 to C96, C132 to C97, C128 to C98, C103 to C99, D9 to D1, D7 to D10, D28 to D11, D17 to D12, D29 to D13, D15 to D14, D16 to D15, D12 to D16, D19 to D17, D50 to D18, D13 to D19, D5 to D2, D47 to D20, D23 to D21, D20 to D23, D21 to D24, D8 to D25, D11 to D26, D72 to D27, D10 to D28, D59 to D29, D18 to D3, D69 to D30, D63 to D31, D39 to D32, D41 to D33, D37 to D34, D36 to D35, D52 to D36, D51 to D37, D40 to D38, D38 to D39, D14 to D4, D42 to D40, D35 to D41, D43 to D42, D44 to D43, D45 to D44, D32 to D45, D49 to D47, D33 to D49, D24 to D5, D58 to D50, D57 to D51, D31 to D52, D30 to D53, D60 to D54, D34 to D55, D62 to D56, D61 to D57, D73 to D58, D68 to D59, D27 to D6, D74 to D60, D65 to D61, D64 to D62, D70 to D63, D67 to D64, D71 to D65, D3 to D67, D4 to D68, D2 to D69, D26 to D7, D1 to D70, D78 to D71, D77 to D72, D75 to D73, D76 to D74, D56 to D75, D55 to D76, D54 to D77, D53 to D78, D25 to D8, D6 to D9, IC6 to IC1, IC17 to IC10, IC16 to IC11, IC14 to IC12, IC15 to IC13, IC11 to IC14, IC12 to IC15, IC13 to IC16, IC10 to IC17, IC9 to IC18, IC7 to IC2, IC8 to IC3, IC5 to IC4, IC3 to IC5, IC2 to IC6, IC4 to IC7, IC1 to IC8, IC18 to IC9, J3 to J1, J7 to J2, J1 to J3, J2 to J4, J4 to J6, J6 to J7, Q10 to Q1, Q6 to Q10, Q1 to Q11, Q5 to Q12, Q3 to Q13, Q7 to Q14, Q23 to Q15, Q25 to Q16, Q27 to Q17, Q22 to Q18, Q24 to Q19, Q11 to Q2, Q26 to Q20, Q28 to Q21, Q15 to Q22, Q16 to Q23, Q18 to Q24, Q20 to Q25, Q19 to Q26, Q17 to Q27, Q21 to Q28, Q12 to Q3, Q14 to Q4, Q13 to Q5, Q9 to Q6, Q8 to Q7, Q4 to Q8, Q2 to Q9, R32 to R1, R30 to R10, R111 to R100, R104 to R101, R86 to R102, R87 to R103, R84 to R104, R79 to R105, R82 to R106, R80 to R107, R89 to R108, R83 to R109, R55 to R11, R88 to R110, R77 to R111, R76 to R112, R85 to R113, R81 to R114, R78 to R115, R48 to R12, R53 to R13, R47 to R14, R54 to R16, R52 to R17, R46 to R18, R26 to R19, R18 to R2, R16 to R22, R22 to R23, R71 to R24, R57 to R25, R73 to R26, R56 to R27, R49 to R28, R50 to R29, R28 to R3, R70 to R30, R33 to R31, R31 to R32, R40 to R33, R51 to R35, R72 to R36, R36 to R37, R39 to R38, R35 to R39, R25 to R4, R42 to R40, R37 to R42, R38 to R43, R92 to R44, R98 to R45, R24 to R46, R23 to R47, R96 to R48, R97 to R49, R45 to R5, R99 to R50, R90 to R51, R91 to R52, R75 to R53, R74 to R54, R66 to R55, R64 to R56, R69 to R57, R67 to R58, R60 to R59, R19 to R6, R68 to R60, R65 to R61, R59 to R62, R61 to R63, R62 to R64, R63 to R65, R58 to R66, R94 to R67, R93 to R68, R95 to R69, R29 to R7, R100 to R70, R101 to R71, R44 to R72, R43 to R73, R7 to R74, R14 to R75, R13 to R76, R11 to R77, R12 to R78, R9 to R79, R17 to R8, R4 to R80, R1 to R81, R5 to R82, R8 to R83, R2 to R84, R113 to R85, R105 to R86, R108 to R87, R10 to R88, R6 to R89, R27 to R9, R109 to R90, R115 to R91, R106 to R92, R114 to R93, R3 to R94, R103 to R95, R112 to R96, R110 to R97, R102 to R98, R107 to R99, TP6 to TP2, TP2 to TP3, TP3 to TP4, TP4 to TP6, U2 to U1, U1 to U2, U6 to U5, U7 to U6, U5 to U7
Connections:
- C105 pad 2: /servo2/HALL_V -> /servo2/HALL_V_FILT
- C106 pad 2: /servo2/HALL_W -> /servo2/HALL_W_FILT
- C107 pad 2: /servo2/HALL_U -> /servo2/HALL_U_FILT
- C122 pad 2: /servo3/HALL_W -> /servo3/HALL_W_FILT
- C123 pad 2: /servo3/HALL_U -> /servo3/HALL_U_FILT
- C124 pad 2: /servo3/HALL_V -> /servo3/HALL_V_FILT
- C61 pad 2: /servo1/HALL_U -> /servo1/HALL_U_FILT
- C66 pad 2: /servo1/HALL_W -> /servo1/HALL_W_FILT
- C69 pad 2: /servo1/HALL_V -> /servo1/HALL_V_FILT
- D21 pad 1: /servo1/HALL_V -> /servo1/HALL_V_FILT
- D22 pad 2: /servo1/HALL_V -> /servo1/HALL_V_FILT
- D23 pad 2: /servo1/HALL_W -> /servo1/HALL_W_FILT
- D24 pad 1: /servo1/HALL_W -> /servo1/HALL_W_FILT
- D42 pad 2: /servo2/HALL_W -> /servo2/HALL_W_FILT
- D43 pad 1: /servo2/HALL_W -> /servo2/HALL_W_FILT
- D44 pad 2: /servo2/HALL_V -> /servo2/HALL_V_FILT
- D46 pad 1: /servo2/HALL_V -> /servo2/HALL_V_FILT
- D47 pad 1: /servo2/HALL_U -> /servo2/HALL_U_FILT
- D48 pad 2: /servo2/HALL_U -> /servo2/HALL_U_FILT
- D59 pad 1: /servo3/HALL_V -> /servo3/HALL_V_FILT
- D61 pad 2: /servo3/HALL_W -> /servo3/HALL_W_FILT
- D63 pad 2: /servo3/HALL_U -> /servo3/HALL_U_FILT
- D64 pad 2: /servo3/HALL_V -> /servo3/HALL_V_FILT
- D65 pad 1: /servo3/HALL_U -> /servo3/HALL_U_FILT
- D66 pad 1: /servo3/HALL_W -> /servo3/HALL_W_FILT
- D7 pad 1: /servo1/HALL_U -> /servo1/HALL_U_FILT
- D8 pad 2: /servo1/HALL_U -> /servo1/HALL_U_FILT
- H1 pad 1: (no net) -> GND
- H2 pad 1: (no net) -> GND
- H3 pad 1: (no net) -> GND
- H4 pad 1: (no net) -> GND
- IC3 pad 11: /IO/INT_IMU3 -> /microcontrollers/INT_IMU3
- J2 pad 10: /servo1/HALL_W -> /motorIO/HALL_C3
- J2 pad 8: /servo1/HALL_V -> /motorIO/HALL_B3
- J2 pad 9: /servo1/HALL_U -> /motorIO/HALL_A3
- J5 pad 10: /servo3/HALL_W -> /motorIO/HALL_C1
- J5 pad 8: /servo3/HALL_V -> /motorIO/HALL_B1
- J5 pad 9: /servo3/HALL_U -> /motorIO/HALL_A1
- J7 pad 10: /servo2/HALL_W -> /motorIO/HALL_C2
- J7 pad 8: /servo2/HALL_V -> /motorIO/HALL_B2
- J7 pad 9: /servo2/HALL_U -> /motorIO/HALL_A2
- R12 pad 2: /servo1/HALL_W -> /motorIO/HALL_C3
- R14 pad 2: /servo1/HALL_V -> /motorIO/HALL_B3
- R18 pad 2: /servo1/HALL_U -> /motorIO/HALL_A3
- R28 pad 1: /servo1/HALL_W -> /motorIO/HALL_C3
- R28 pad 2: /servo1/HALL_W -> /servo1/HALL_W_FILT
- R29 pad 1: /servo1/HALL_V -> /motorIO/HALL_B3
- R29 pad 2: /servo1/HALL_V -> /servo1/HALL_V_FILT
- R35 pad 1: /servo1/HALL_U -> /motorIO/HALL_A3
- R35 pad 2: /servo1/HALL_U -> /servo1/HALL_U_FILT
- R44 pad 2: /servo3/HALL_W -> /motorIO/HALL_C1
- R51 pad 2: /servo3/HALL_U -> /motorIO/HALL_A1
- R52 pad 2: /servo3/HALL_V -> /motorIO/HALL_B1
- R55 pad 2: /servo2/HALL_W -> /motorIO/HALL_C2
- R56 pad 2: /servo2/HALL_U -> /motorIO/HALL_A2
- R57 pad 1: /servo2/HALL_U -> /motorIO/HALL_A2
- R57 pad 2: /servo2/HALL_U -> /servo2/HALL_U_FILT
- R58 pad 1: /servo2/HALL_W -> /motorIO/HALL_C2
- R58 pad 2: /servo2/HALL_W -> /servo2/HALL_W_FILT
- R60 pad 1: /servo2/HALL_V -> /motorIO/HALL_B2
- R60 pad 2: /servo2/HALL_V -> /servo2/HALL_V_FILT
- R61 pad 2: /servo2/HALL_V -> /motorIO/HALL_B2
- R67 pad 1: /servo3/HALL_V -> /motorIO/HALL_B1
- R67 pad 2: /servo3/HALL_V -> /servo3/HALL_V_FILT
- R68 pad 1: /servo3/HALL_W -> /motorIO/HALL_C1
- R68 pad 2: /servo3/HALL_W -> /servo3/HALL_W_FILT
- R69 pad 1: /servo3/HALL_U -> /motorIO/HALL_A1
- R69 pad 2: /servo3/HALL_U -> /servo3/HALL_U_FILT
- U4 pad 36: /servo1/HALL_W -> /servo1/HALL_W_FILT
- U4 pad 37: /servo1/HALL_V -> /servo1/HALL_V_FILT
- U4 pad 38: /servo1/HALL_U -> /servo1/HALL_U_FILT
- U5 pad 36: /servo2/HALL_W -> /servo2/HALL_W_FILT
- U5 pad 37: /servo2/HALL_V -> /servo2/HALL_V_FILT
- U5 pad 38: /servo2/HALL_U -> /servo2/HALL_U_FILT
- U6 pad 36: /servo3/HALL_W -> /servo3/HALL_W_FILT
- U6 pad 37: /servo3/HALL_V -> /servo3/HALL_V_FILT
- U6 pad 38: /servo3/HALL_U -> /servo3/HALL_U_FILT
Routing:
- net +3.3V: track 0.00 -> 184.4 mm
- net +5V: track 0.00 -> 82.0 mm, vias 0 -> 6
- net +2.5V: track 0.00 -> 69.9 mm
- net Net-(IC1-ACP): track 0.00 -> 36.2 mm, vias 0 -> 2
- net Net-(Q6-G): track 0.00 -> 30.8 mm
- net /voltageregulators/SW1: track 0.00 -> 24.9 mm
- net /voltageregulators/SW2: track 0.00 -> 22.9 mm
- net /servo1/HALL_W_FILT: track 0.00 -> 20.4 mm, vias 0 -> 2
- net /servo3/HALL_W_FILT: track 0.00 -> 20.4 mm, vias 0 -> 2
- net /servo2/HALL_W_FILT: track 0.00 -> 20.4 mm, vias 0 -> 2
- net /servo1/ADC_I0_POS: track 0.00 -> 20.0 mm
- net /servo3/ADC_I0_POS: track 0.00 -> 20.0 mm
- net /servo2/ADC_I0_POS: track 0.00 -> 20.0 mm
- net /IO/SWDIO: track 0.00 -> 18.5 mm, vias 0 -> 2
- net /servo1/HALL_V_FILT: track 0.00 -> 18.0 mm, vias 0 -> 2
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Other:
- board size 140 x 140 mm -> 122 x 122 mm
